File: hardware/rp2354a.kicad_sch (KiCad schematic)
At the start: 28 parts, among them SW1 RESET, SW2 BOOTSEL, U3 RP2354A, Y1 12MHz

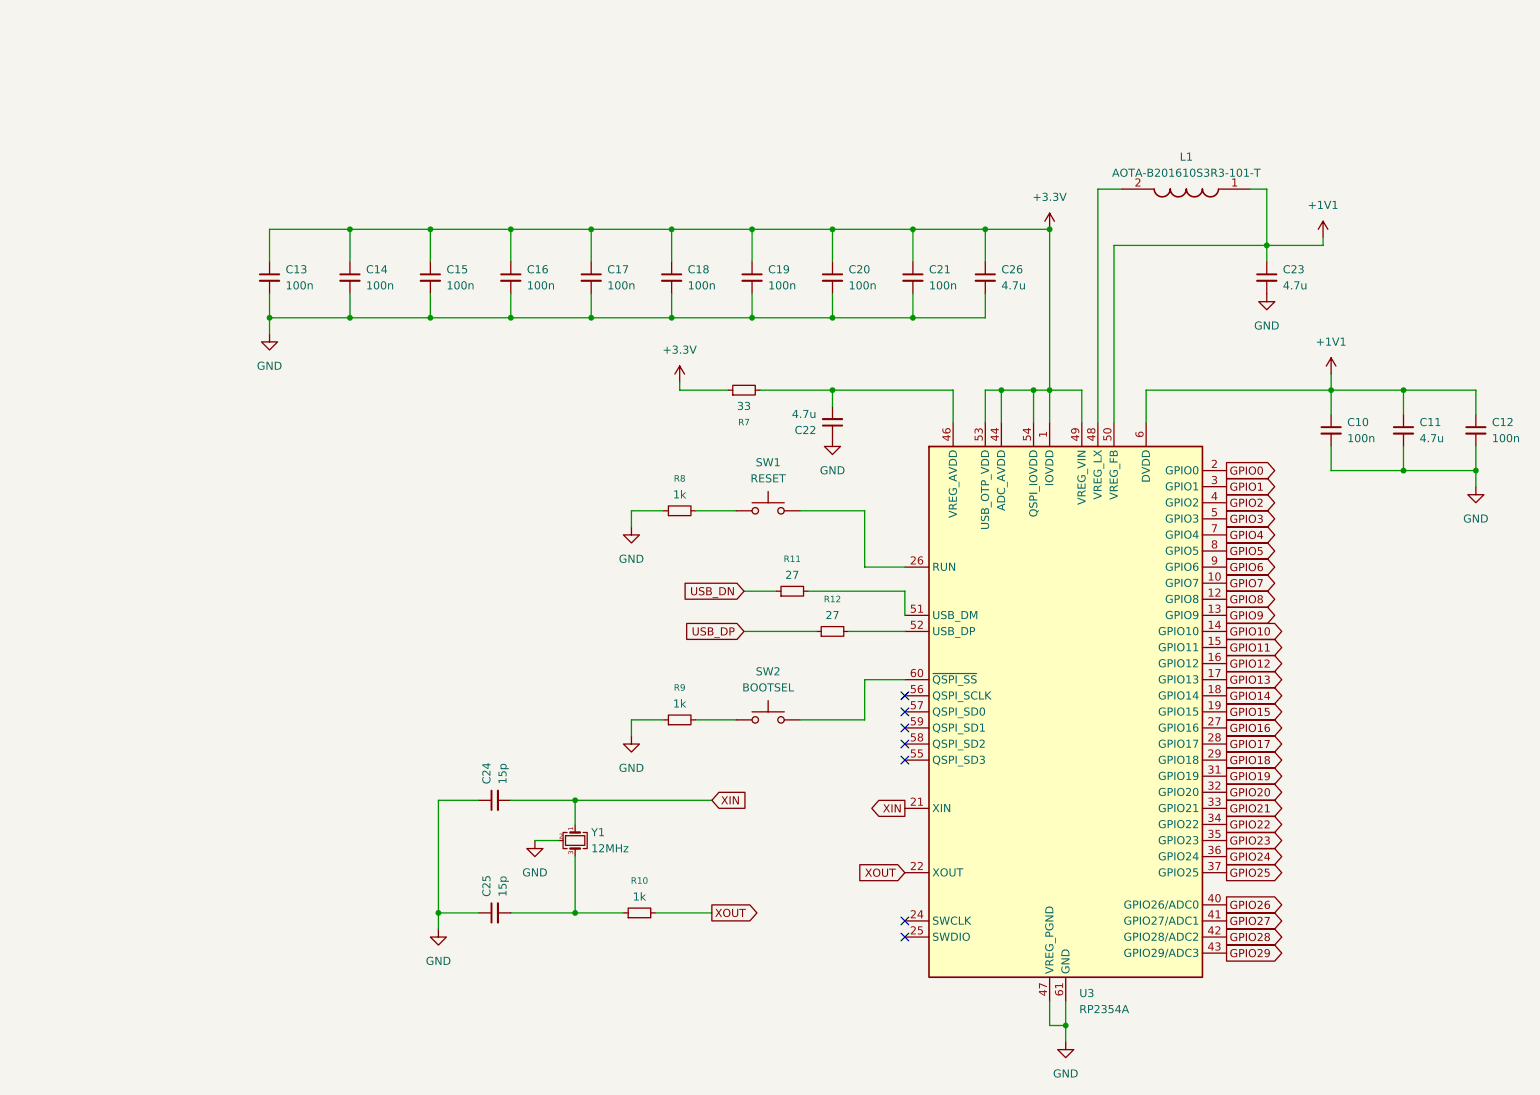
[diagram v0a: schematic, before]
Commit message: separate left/right part design, schematic
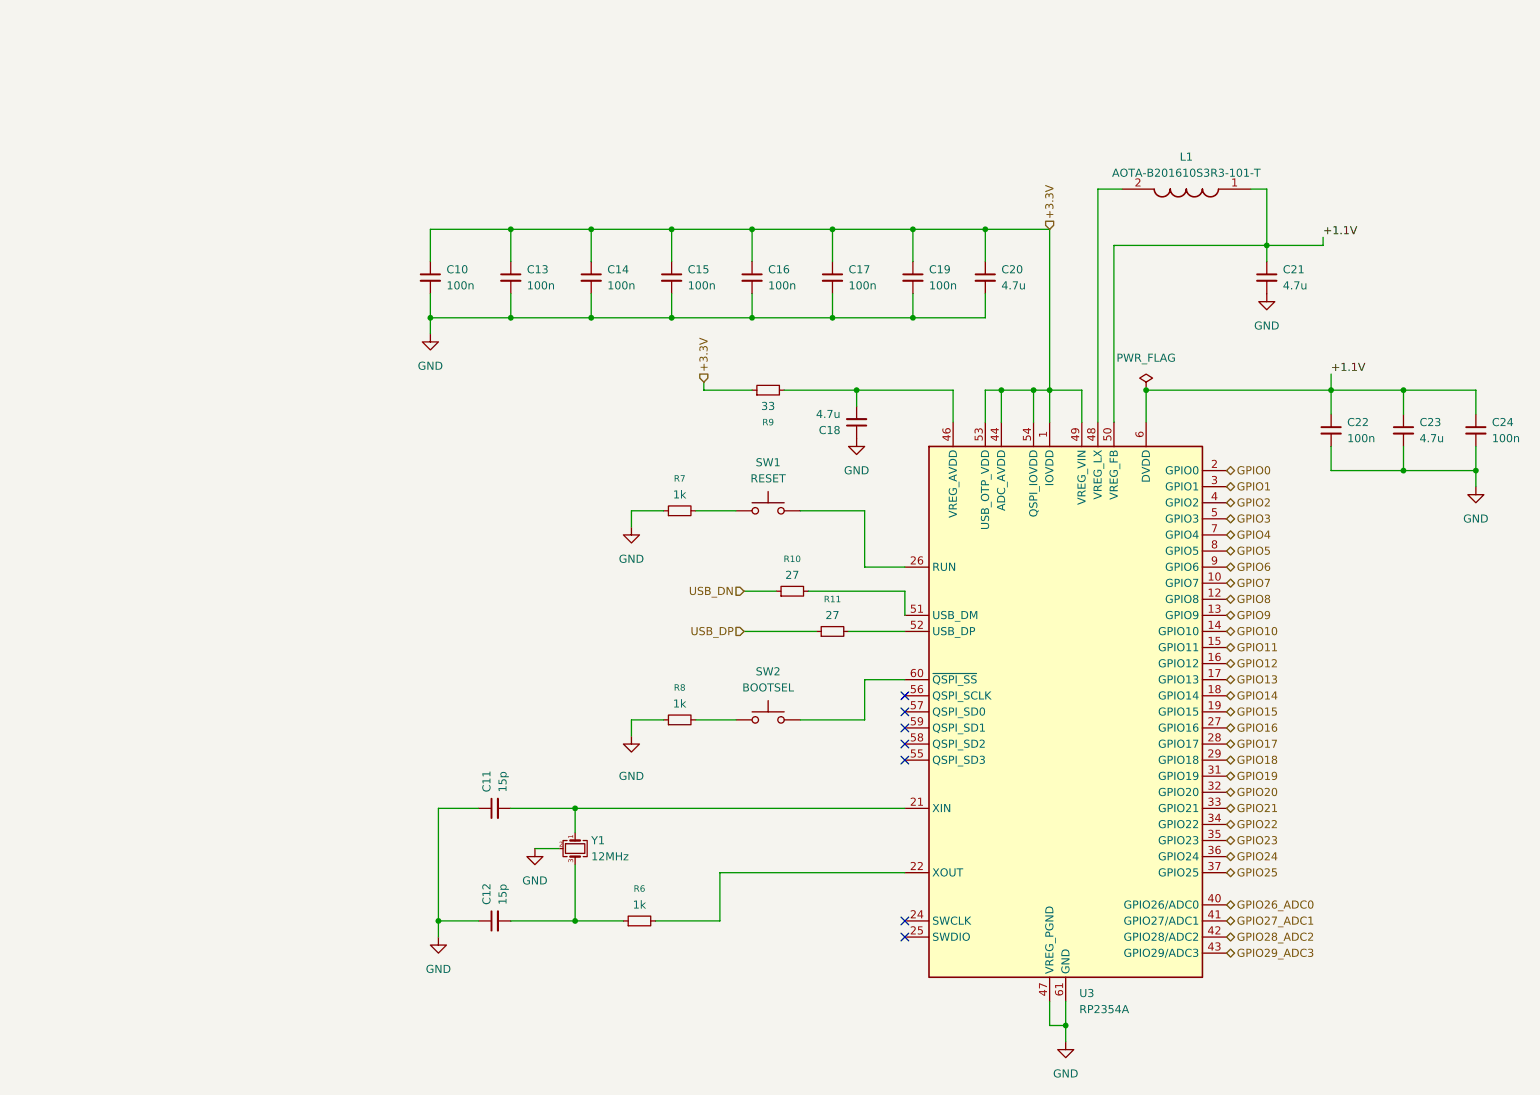
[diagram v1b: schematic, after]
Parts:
- removed C14, C15: 100n, PCM_Capacitor_SMD_AKL:C_0402_1005Metric_Pad0.74x0.62mm_HandSolder, symbol Device:C_Small
- C10: renamed from C13; footprint PCM_Capacitor_SMD_AKL:C_0402_1005Metric_Pad0.74x0.62mm_HandSolder -> PCM_Capacitor_SMD_AKL:C_0402_1005Metric
- C11: renamed from C24; footprint PCM_Capacitor_SMD_AKL:C_0603_1608Metric_Pad1.05x0.95mm_HandSolder -> PCM_Capacitor_SMD_AKL:C_0402_1005Metric
- C12: renamed from C25; footprint PCM_Capacitor_SMD_AKL:C_0603_1608Metric_Pad1.05x0.95mm_HandSolder -> PCM_Capacitor_SMD_AKL:C_0402_1005Metric
- C13: renamed from C16; footprint PCM_Capacitor_SMD_AKL:C_0402_1005Metric_Pad0.74x0.62mm_HandSolder -> PCM_Capacitor_SMD_AKL:C_0402_1005Metric
- C14: renamed from C17; footprint PCM_Capacitor_SMD_AKL:C_0402_1005Metric_Pad0.74x0.62mm_HandSolder -> PCM_Capacitor_SMD_AKL:C_0402_1005Metric
- C15: renamed from C18; footprint PCM_Capacitor_SMD_AKL:C_0402_1005Metric_Pad0.74x0.62mm_HandSolder -> PCM_Capacitor_SMD_AKL:C_0402_1005Metric
- C16: renamed from C19; footprint PCM_Capacitor_SMD_AKL:C_0402_1005Metric_Pad0.74x0.62mm_HandSolder -> PCM_Capacitor_SMD_AKL:C_0402_1005Metric
- C17: renamed from C20; footprint PCM_Capacitor_SMD_AKL:C_0402_1005Metric_Pad0.74x0.62mm_HandSolder -> PCM_Capacitor_SMD_AKL:C_0402_1005Metric
- C18: renamed from C22; footprint PCM_Capacitor_SMD_AKL:C_0402_1005Metric_Pad0.74x0.62mm_HandSolder -> PCM_Capacitor_SMD_AKL:C_0402_1005Metric
- C19: renamed from C21; footprint PCM_Capacitor_SMD_AKL:C_0402_1005Metric_Pad0.74x0.62mm_HandSolder -> PCM_Capacitor_SMD_AKL:C_0402_1005Metric
- C20: renamed from C26; footprint PCM_Capacitor_SMD_AKL:C_0402_1005Metric_Pad0.74x0.62mm_HandSolder -> PCM_Capacitor_SMD_AKL:C_0402_1005Metric
- C21: renamed from C23; footprint PCM_Capacitor_SMD_AKL:C_0402_1005Metric_Pad0.74x0.62mm_HandSolder -> PCM_Capacitor_SMD_AKL:C_0402_1005Metric
- C22: renamed from C10; footprint PCM_Capacitor_SMD_AKL:C_0402_1005Metric_Pad0.74x0.62mm_HandSolder -> PCM_Capacitor_SMD_AKL:C_0402_1005Metric
- C23: renamed from C11; footprint PCM_Capacitor_SMD_AKL:C_0402_1005Metric_Pad0.74x0.62mm_HandSolder -> PCM_Capacitor_SMD_AKL:C_0402_1005Metric
- C24: renamed from C12; footprint PCM_Capacitor_SMD_AKL:C_0402_1005Metric_Pad0.74x0.62mm_HandSolder -> PCM_Capacitor_SMD_AKL:C_0402_1005Metric
- L1: footprint AOTAB201610S3R3101T -> rp_voyager:INDC2016X100N
- R10: renamed from R11; footprint Resistor_SMD:R_0603_1608Metric_Pad0.98x0.95mm_HandSolder -> PCM_Resistor_SMD_AKL:R_0402_1005Metric_Pad0.72x0.64mm_HandSolder
- R11: renamed from R12; footprint Resistor_SMD:R_0603_1608Metric_Pad0.98x0.95mm_HandSolder -> PCM_Resistor_SMD_AKL:R_0402_1005Metric_Pad0.72x0.64mm_HandSolder
- R6: renamed from R10; footprint Resistor_SMD:R_0603_1608Metric_Pad0.98x0.95mm_HandSolder -> PCM_Resistor_SMD_AKL:R_0402_1005Metric_Pad0.72x0.64mm_HandSolder
- R7: renamed from R8; footprint Resistor_SMD:R_0603_1608Metric_Pad0.98x0.95mm_HandSolder -> PCM_Resistor_SMD_AKL:R_0603_1608Metric_Pad0.98x0.95mm_HandSolder
- R8: renamed from R9; footprint Resistor_SMD:R_0603_1608Metric_Pad0.98x0.95mm_HandSolder -> PCM_Resistor_SMD_AKL:R_0603_1608Metric_Pad0.98x0.95mm_HandSolder
- R9: renamed from R7; footprint PCM_Resistor_SMD_AKL:R_0201_0603Metric_Pad0.64x0.40mm_HandSolder -> PCM_Resistor_SMD_AKL:R_0402_1005Metric_Pad0.72x0.64mm_HandSolder
- SW1: footprint Button_Switch_SMD:SW_SPST_CK_RS282G05A3 -> Button_Switch_SMD:SW_Push_SPST_NO_Alps_SKRK
- SW2: footprint (none) -> Button_Switch_SMD:SW_Push_SPST_NO_Alps_SKRK
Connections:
- net +1V1 renamed +1.1V
- net GPIO26 renamed GPIO26_ADC0
- net GPIO27 renamed GPIO27_ADC1
- net GPIO28 renamed GPIO28_ADC2
- net GPIO29 renamed GPIO29_ADC3
- net XIN: no longer names the net of C11.2, U3.21 (XIN), Y1.1
- net XOUT: no longer names the net of R6.2, U3.22 (XOUT)
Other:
- moved on the sheet: C10, C11, C12, C18, R6, R9, Y1

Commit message: electronics
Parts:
- C11: renamed from C10; footprint PCM_Capacitor_SMD_AKL:C_0402_1005Metric -> PCM_Capacitor_SMD_Handsoldering_AKL:C_0402_1005Metric
- C12: renamed from C11; footprint PCM_Capacitor_SMD_AKL:C_0402_1005Metric -> PCM_Capacitor_SMD_Handsoldering_AKL:C_0402_1005Metric
- C13: renamed from C12; footprint PCM_Capacitor_SMD_AKL:C_0402_1005Metric -> PCM_Capacitor_SMD_Handsoldering_AKL:C_0402_1005Metric
- C14: renamed from C13; footprint PCM_Capacitor_SMD_AKL:C_0402_1005Metric -> PCM_Capacitor_SMD_Handsoldering_AKL:C_0402_1005Metric
- C15: renamed from C14; footprint PCM_Capacitor_SMD_AKL:C_0402_1005Metric -> PCM_Capacitor_SMD_Handsoldering_AKL:C_0402_1005Metric
- C16: renamed from C15; footprint PCM_Capacitor_SMD_AKL:C_0402_1005Metric -> PCM_Capacitor_SMD_Handsoldering_AKL:C_0402_1005Metric
- C17: renamed from C16; footprint PCM_Capacitor_SMD_AKL:C_0402_1005Metric -> PCM_Capacitor_SMD_Handsoldering_AKL:C_0402_1005Metric
- C18: renamed from C17; footprint PCM_Capacitor_SMD_AKL:C_0402_1005Metric -> PCM_Capacitor_SMD_Handsoldering_AKL:C_0402_1005Metric
- C19: renamed from C18; footprint PCM_Capacitor_SMD_AKL:C_0402_1005Metric -> PCM_Capacitor_SMD_Handsoldering_AKL:C_0402_1005Metric
- C20: renamed from C19; footprint PCM_Capacitor_SMD_AKL:C_0402_1005Metric -> PCM_Capacitor_SMD_Handsoldering_AKL:C_0402_1005Metric
- C21: renamed from C20; footprint PCM_Capacitor_SMD_AKL:C_0402_1005Metric -> PCM_Capacitor_SMD_Handsoldering_AKL:C_0402_1005Metric
- C22: renamed from C21; footprint PCM_Capacitor_SMD_AKL:C_0402_1005Metric -> PCM_Capacitor_SMD_Handsoldering_AKL:C_0402_1005Metric
- C23: renamed from C22; footprint PCM_Capacitor_SMD_AKL:C_0402_1005Metric -> PCM_Capacitor_SMD_Handsoldering_AKL:C_0402_1005Metric
- C24: renamed from C23; footprint PCM_Capacitor_SMD_AKL:C_0402_1005Metric -> PCM_Capacitor_SMD_Handsoldering_AKL:C_0402_1005Metric
- C25: renamed from C24; footprint PCM_Capacitor_SMD_AKL:C_0402_1005Metric -> PCM_Capacitor_SMD_Handsoldering_AKL:C_0402_1005Metric
- L1: Distributor Link 1 (none) -> https://hu.mouser.com/ProductDetail/815-AB201610S3R3101T; Manufacturer (none) -> ABRACON
- R11: renamed from R6; footprint PCM_Resistor_SMD_AKL:R_0402_1005Metric_Pad0.72x0.64mm_HandSolder -> PCM_Resistor_SMD_AKL:R_0402_1005Metric; Distributor Link 3 (none) -> https://www.hestore.hu/prod_10030528.html
- R12: renamed from R7; footprint PCM_Resistor_SMD_AKL:R_0603_1608Metric_Pad0.98x0.95mm_HandSolder -> PCM_Resistor_SMD_AKL:R_0603_1608Metric; Distributor Link 3 (none) -> https://www.hestore.hu/prod_10049434.html
- R13: renamed from R8; footprint PCM_Resistor_SMD_AKL:R_0603_1608Metric_Pad0.98x0.95mm_HandSolder -> PCM_Resistor_SMD_AKL:R_0603_1608Metric; Distributor Link 3 (none) -> https://www.hestore.hu/prod_10049434.html
- R14: renamed from R9; footprint PCM_Resistor_SMD_AKL:R_0402_1005Metric_Pad0.72x0.64mm_HandSolder -> PCM_Resistor_SMD_AKL:R_0402_1005Metric; Distributor Link 1 (none) -> https://hu.mouser.com/ProductDetail/YAGEO/RC0402FR-7D33RL?q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
- R15: renamed from R10; footprint PCM_Resistor_SMD_AKL:R_0402_1005Metric_Pad0.72x0.64mm_HandSolder -> PCM_Resistor_SMD_AKL:R_0402_1005Metric; Distributor Link 1 (none) -> https://hu.mouser.com/ProductDetail/YAGEO/RC0402FR-0727RL?q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
- R16: renamed from R11; footprint PCM_Resistor_SMD_AKL:R_0402_1005Metric_Pad0.72x0.64mm_HandSolder -> PCM_Resistor_SMD_AKL:R_0402_1005Metric; Distributor Link 1 (none) -> https://hu.mouser.com/ProductDetail/YAGEO/RC0402FR-0727RL?q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
- Y1: Manufacturer (none) -> ABRACON
